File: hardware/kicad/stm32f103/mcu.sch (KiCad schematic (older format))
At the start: 14 parts, among them P10 SWD, P8 UART, P9 I2C, SW3 RESET, U2 STM32F030F4Px, Y1 12MHz

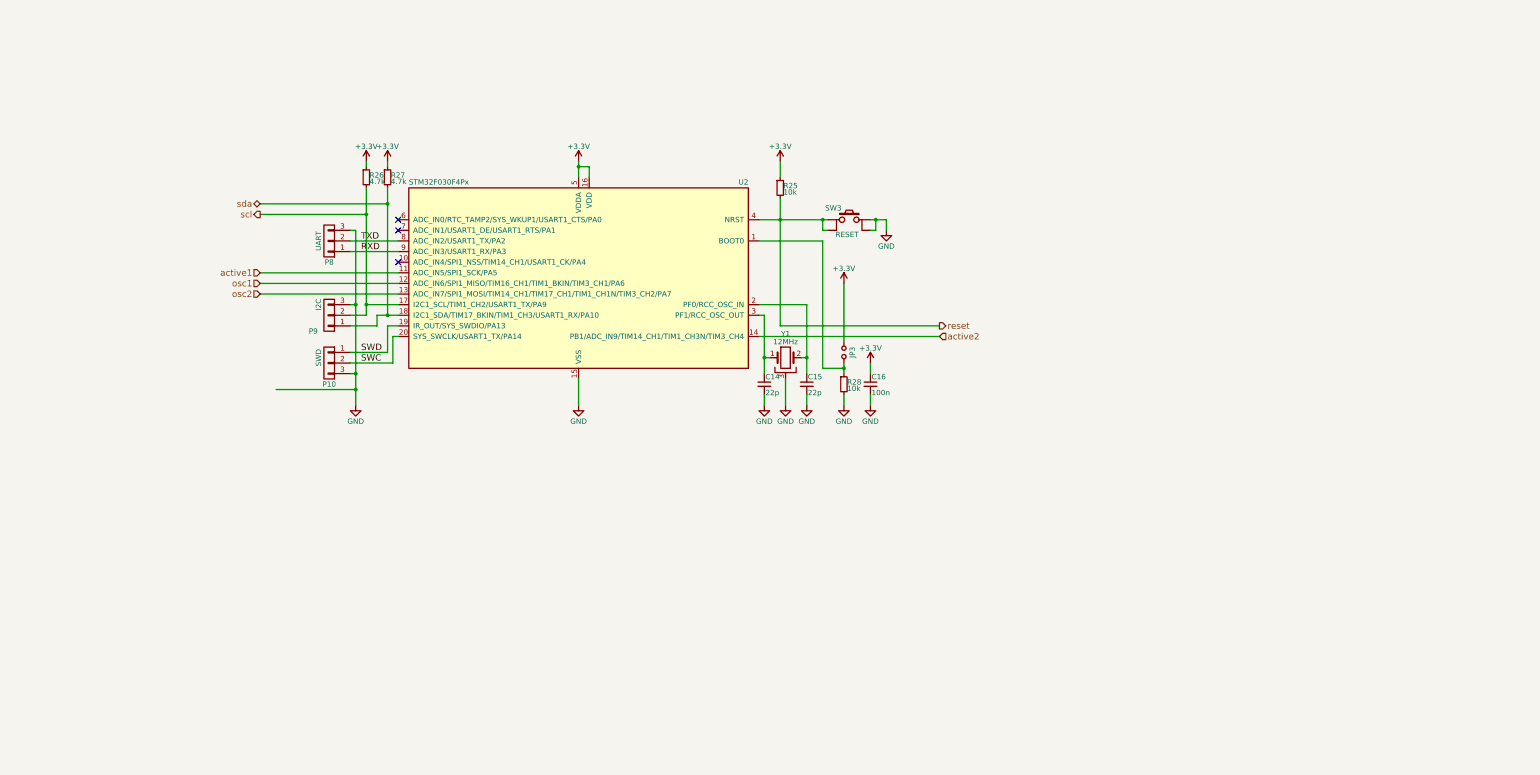
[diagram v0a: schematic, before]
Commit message: hardware/kicad/stm32f103: MCU/LED block ready
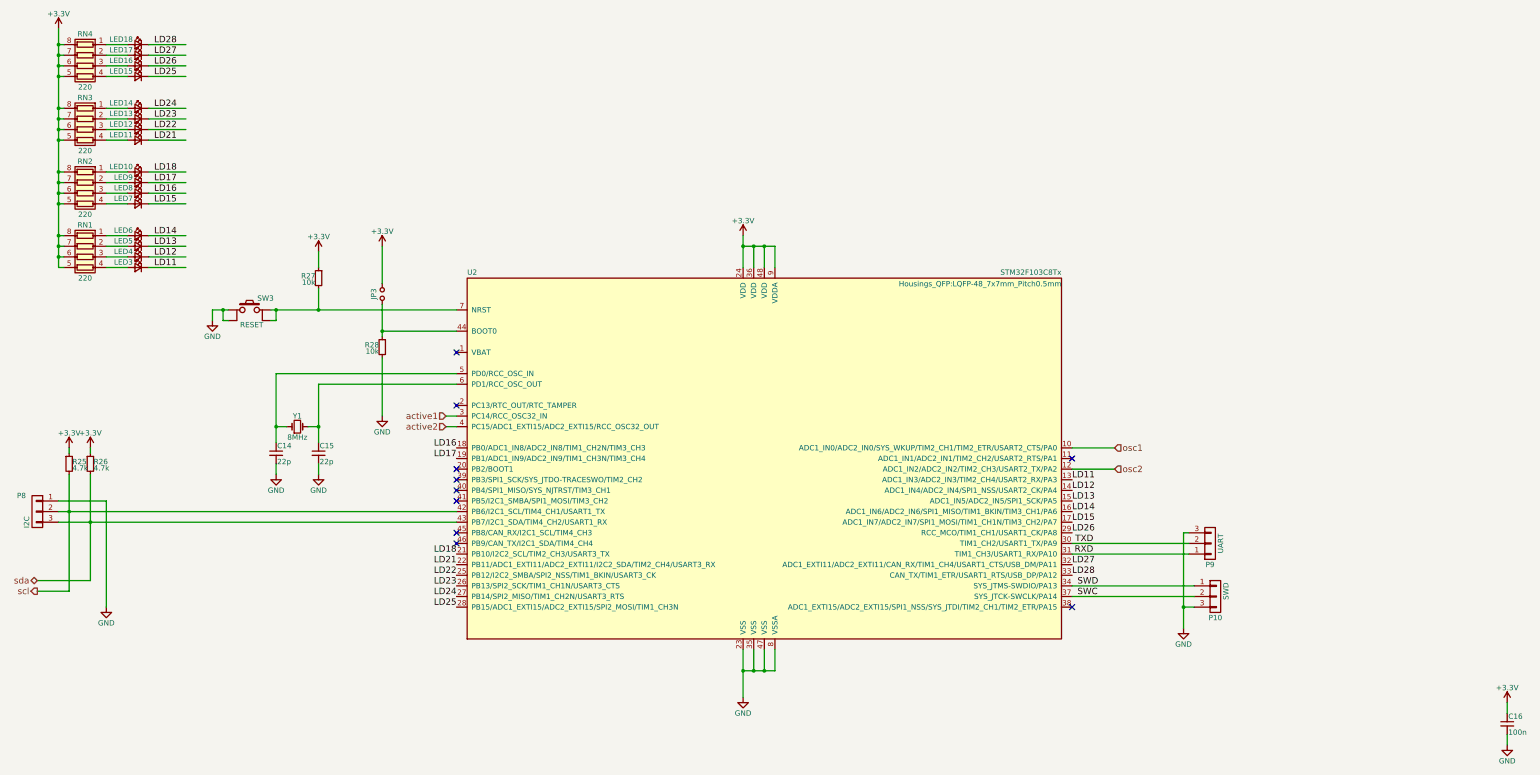
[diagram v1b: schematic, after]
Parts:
- removed U2: STM32F030F4Px, Housings_SSOP:TSSOP-20_4.4x6.5mm_Pitch0.65mm_Handsoldering, symbol STM32F030F4Px
- removed Y1: 12MHz, Crystals:Crystal_SMD_3225_4Pads, symbol Crystal_GND3
- added LED10, LED11, LED12, LED13, LED14, LED15, LED16, LED17, LED18, LED3, LED4, LED5, LED6, LED7, LED8, LED9: LED_Small, LEDs:LED_0805, symbol LED_Small
- added RN1, RN2, RN3, RN4: 220, Resistors_SMD:R_Array_Convex_4x0603_HandSoldering, symbol R_Pack04
- added U2: STM32F103C8Tx, Housings_QFP:LQFP-48_7x7mm_Pitch0.5mm, symbol STM32F103C8Tx
- added Y1: 8MHz, Crystals:Crystal_HC49-U_Vertical, symbol Crystal_Small
- renumbered P9 to P8, P8 to P9, R26 to R25, R27 to R26, R25 to R27
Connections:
- net labels added: LD11, LD12, LD13, LD14, LD15, LD16, LD17, LD18, LD21, LD22, LD23, LD24, LD25, LD26, LD27, LD28
- net labels removed: reset
- wire segments 59 -> 103
- no-connect marks 3 -> 10
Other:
- moved on the sheet: C14, C15, C16, JP3, P10, P8, P9, R25, R26, R27, R28, SW3

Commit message: hardware/kicad/stm32f103: Minor cosmetic changes
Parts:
- removed JP3: boot0, Pin_Headers:Pin_Header_Straight_1x02_Pitch2.54mm, symbol Jumper_NO_Small
- removed R28: 10k, Resistors_SMD:R_0603_HandSoldering, symbol R_Small
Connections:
- wire segments 103 -> 101
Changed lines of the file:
@@
 L GND #PWR038
 U 1 1 5884DF65
-P 4200 5000
-F 0 "#PWR038" H 4200 4750 50  0001 C CNN
-F 1 "GND" H 4200 4850 50  0000 C CNN
-F 2 "" H 4200 5000 50  0000 C CNN
-F 3 "" H 4200 5000 50  0000 C CNN
-	1    4200 5000
+P 4750 4250
+F 0 "#PWR038" H 4750 4000 50  0001 C CNN
+F 1 "GND" H 4750 4100 50  0000 C CNN
+F 2 "" H 4750 4250 50  0000 C CNN
+F 3 "" H 4750 4250 50  0000 C CNN
+	1    4750 4250
 	-1   0    0    -1
 $EndComp
@@
 	1    0    0    -1
 $EndComp
-$Comp
-L +3.3V #PWR044
-U 1 1 5885595B
-P 4200 3400
-F 0 "#PWR044" H 4200 3250 50  0001 C CNN
-F 1 "+3.3V" H 4200 3540 50  0000 C CNN
-F 2 "" H 4200 3400 50  0000 C CNN
-F 3 "" H 4200 3400 50  0000 C CNN
-	1    4200 3400
-	-1   0    0    -1
-$EndComp
-$Comp
-L R_Small R28
-U 1 1 58869728
-P 4200 4350
-F 0 "R28" H 4230 4370 50  0000 L CNN
-F 1 "10k" H 4230 4310 50  0000 L CNN
-F 2 "Resistors_SMD:R_0603_HandSoldering" H 4200 4350 50  0001 C CNN
-F 3 "" H 4200 4350 50  0000 C CNN
-	1    4200 4350
-	-1   0    0    -1
-$EndComp
-$Comp
-L Jumper_NO_Small JP3
-U 1 1 58869799
-P 4200 3850
-F 0 "JP3" H 4200 3930 50  0000 C CNN
-F 1 "boot0" H 4210 3790 50  0001 C CNN
-F 2 "Pin_Headers:Pin_Header_Straight_1x02_Pitch2.54mm" H 4200 3850 50  0001 C CNN
-F 3 "" H 4200 3850 50  0000 C CNN
-	1    4200 3850
-	0    -1   1    0
-$EndComp
 Text Label 10900 6300 2    60   ~ 0
 RXD
@@
 Wire Wire Line
 	1450 5300 1450 5350
-Wire Wire Line
-	4200 3400 4200 3750
-Wire Wire Line
-	4200 3950 4200 4250
-Wire Wire Line
-	4200 5000 4200 4450
-Wire Wire Line
-	4200 4200 4900 4200
-Connection ~ 4200 4200
 Wire Wire Line
 	2600 4000 2750 4000
@@
 Connection ~ 1150 1700
 $Comp
-L +3.3V #PWR045
+L +3.3V #PWR044
 U 1 1 58A41E64
 P 1150 1350
-F 0 "#PWR045" H 1150 1200 50  0001 C CNN
+F 0 "#PWR044" H 1150 1200 50  0001 C CNN
 F 1 "+3.3V" H 1150 1490 50  0000 C CNN
 F 2 "" H 1150 1350 50  0000 C CNN
@@
 	1150 6000 4900 6000
 $Comp
-L GND #PWR046
+L GND #PWR045
 U 1 1 58A4597C
 P 1600 6800
-F 0 "#PWR046" H 1600 6550 50  0001 C CNN
+F 0 "#PWR045" H 1600 6550 50  0001 C CNN
 F 1 "GND" H 1600 6650 50  0000 C CNN
 F 2 "" H 1600 6800 50  0000 C CNN
@@
 Text Label 2050 1500 0    60   ~ 0
 LD28
-Text Label 10700 6500 0    60   ~ 0
+Text Label 10700 6400 0    60   ~ 0
 LD28
-Text Label 10700 6400 0    60   ~ 0
+Text Label 10700 6100 0    60   ~ 0
 LD27
 Wire Wire Line
 	11100 5300 10700 5300
-Text Label 10700 6100 0    60   ~ 0
+Text Label 4900 6800 2    60   ~ 0
 LD26
 Text Label 10700 6000 0    60   ~ 0
@@
 Text Label 10700 5700 0    60   ~ 0
 LD12
-Text Label 4900 6400 2    60   ~ 0
+Text Label 4900 6300 2    60   ~ 0
 LD21
-Text Label 4900 6300 2    60   ~ 0
+Text Label 4900 5500 2    60   ~ 0
 LD18
 Text Label 4900 5400 2    60   ~ 0
@@
 Text Label 4900 5300 2    60   ~ 0
 LD16
-Text Label 4900 6800 2    60   ~ 0
+Text Label 4900 6700 2    60   ~ 0
 LD25
-Text Label 4900 6700 2    60   ~ 0
+Text Label 4900 6600 2    60   ~ 0
 LD24
-Text Label 4900 6600 2    60   ~ 0
+Text Label 4900 6500 2    60   ~ 0
 LD23
-Text Label 4900 6500 2    60   ~ 0
+Text Label 4900 6400 2    60   ~ 0
 LD22
 Text Label 10700 5600 0    60   ~ 0
@@
 NoConn ~ 4900 5700
 NoConn ~ 4900 5600
-NoConn ~ 4900 5500
 NoConn ~ 4900 4900
 NoConn ~ 4900 4400
@@
 	1    0    0    -1
 $EndComp
+Wire Wire Line
+	4900 4200 4750 4200
+Wire Wire Line
+	4750 4200 4750 4250
+NoConn ~ 10700 6500
 $EndSCHEMATC
